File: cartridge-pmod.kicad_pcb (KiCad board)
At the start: 2 copper layers, 56 x 20 mm, 25 parts, among them J1 2.54-2*6P Bend insert, J2 CONFIG, J3 PJ-320B, U1 W25Q128JVSIM, U2 878-APS6404L-3SQR-SN, U4 74LVCE1G126SE-7

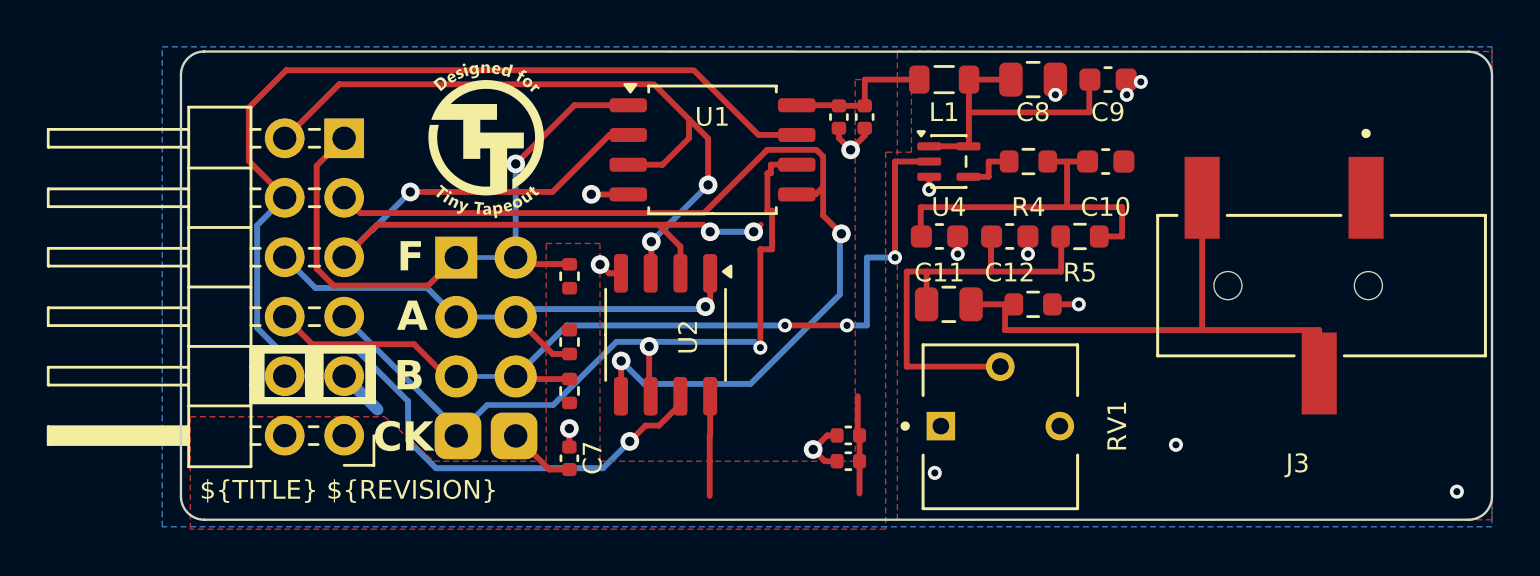
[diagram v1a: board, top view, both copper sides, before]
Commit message: Silk cleanup + J1 promoted to JLC-assembled
- Delete J1's 24 off-board silk pin drawings (18 silk_edge_clearance
  warnings -> 0; fab would clip them, connector body covers the area)
- Nudge C11/C12/R5 label row off C13's pads; un-hide C13 and R6 labels
- Clear DNP on J1 (board + schematic): C60565 header now in JLC BOM/CPL
  for economic THT assembly; J2 stays DNP (solder-jumper pattern)
- Regenerate production/ via headless Fabrication Toolkit (-t -f -e -nI)
- FABRICATION.md: document new J1 status + headless export recipe

DRC after: 0 unconnected, 0 silk, only the 23 known-ignorable baseline
errors (22 CONFIG cut-trace + 1 upstream starved thermal). ERC 0.

Co-Authored-By: Claude Fable 5 <noreply@anthropic.com>
Claude-Session: https://claude.ai/code/session_01KoqFR2y5XeXxq4PQckdZZA
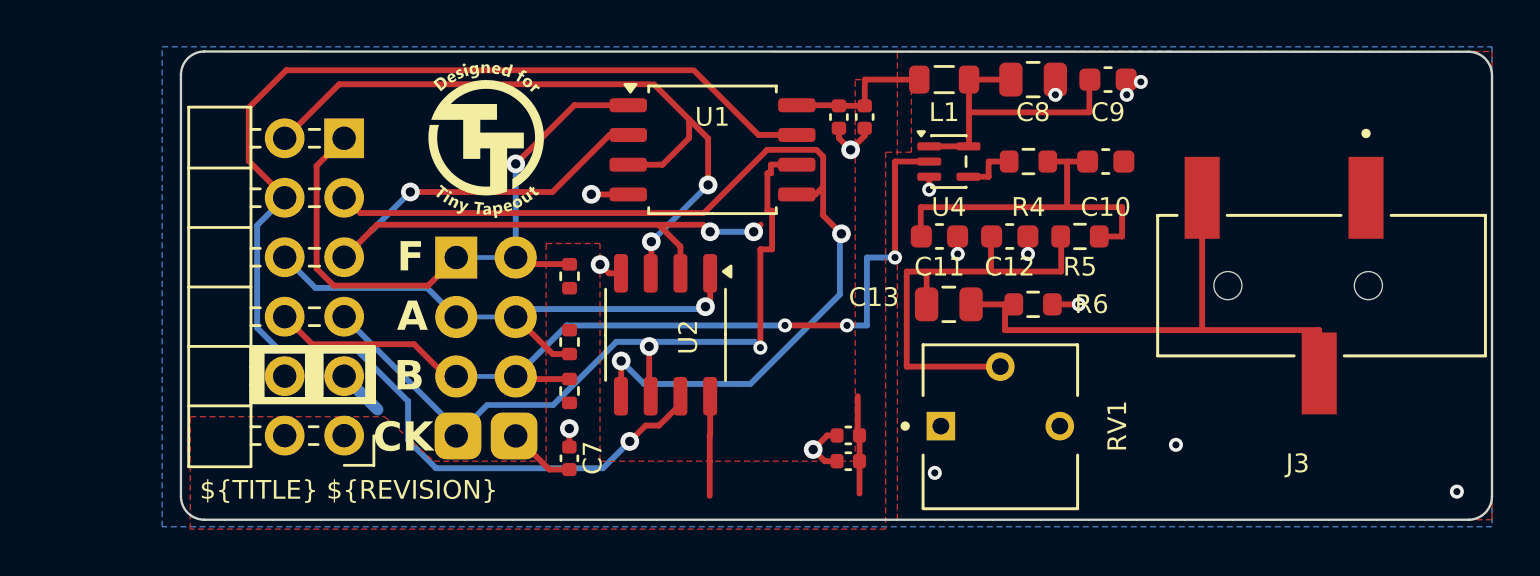
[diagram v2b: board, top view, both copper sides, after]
